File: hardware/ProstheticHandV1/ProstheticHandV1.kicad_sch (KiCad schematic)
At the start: 19 parts, among them J1 Servo_01, J2 Servo_02, J3 Servo_03, J4 Servo_04, J5 JTAG, J6 Bat_Con, J7 OLED_Disp, SW1 Button_01, SW2 Button_02, U1 LM7805_TO220

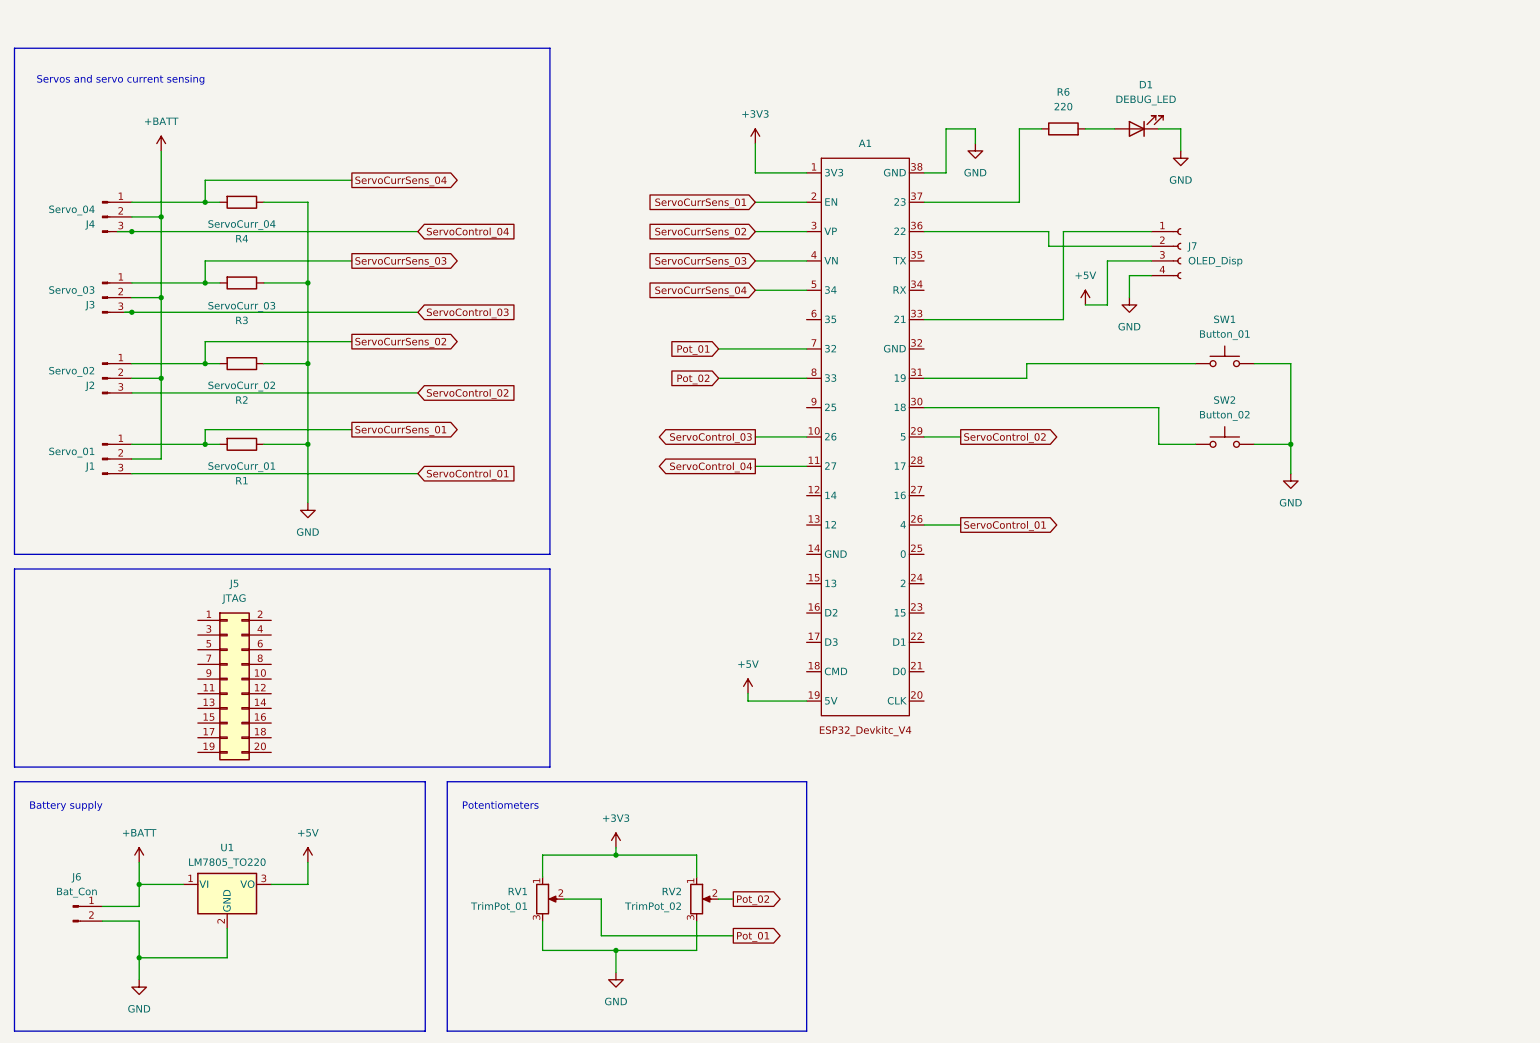
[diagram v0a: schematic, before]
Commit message: KiCAD: Create symbol and footprint for ESP32 S3
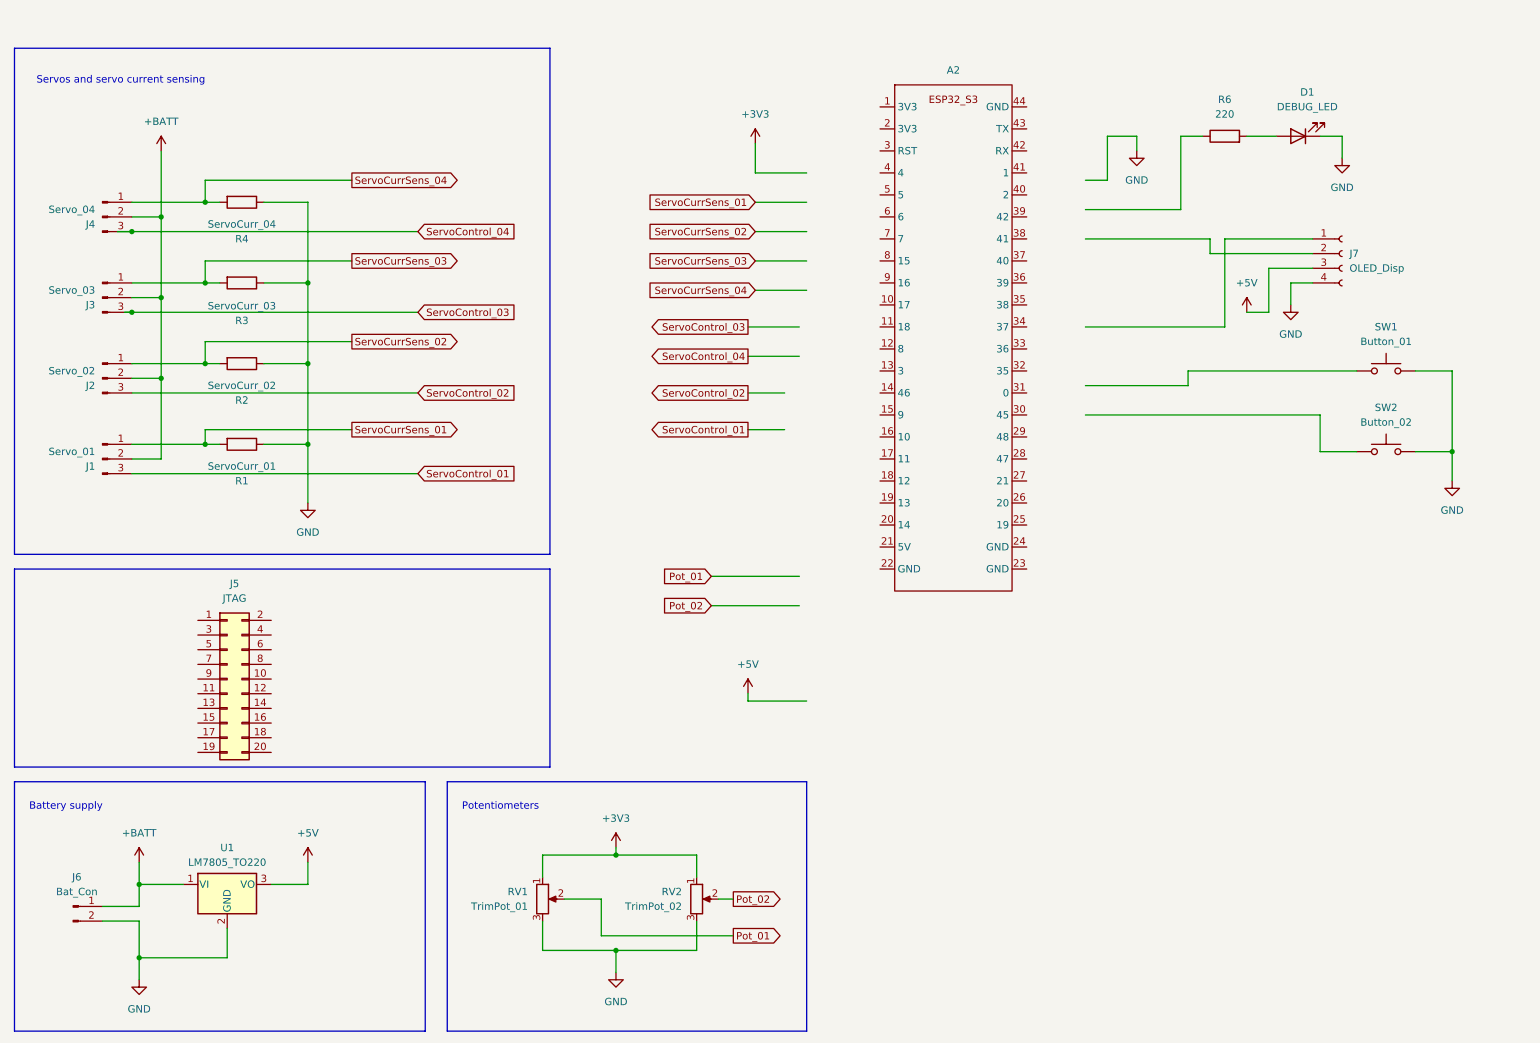
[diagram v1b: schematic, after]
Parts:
- removed A1: ~, symbol ComponentLibrary:ESP32_Devkitc_V4
- added A2: ~, symbol ComponentLibrary:ESP32_S3_DevKitC_V1
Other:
- moved on the sheet: D1, J7, R6, SW1, SW2

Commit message: Started PCB design for hand V1
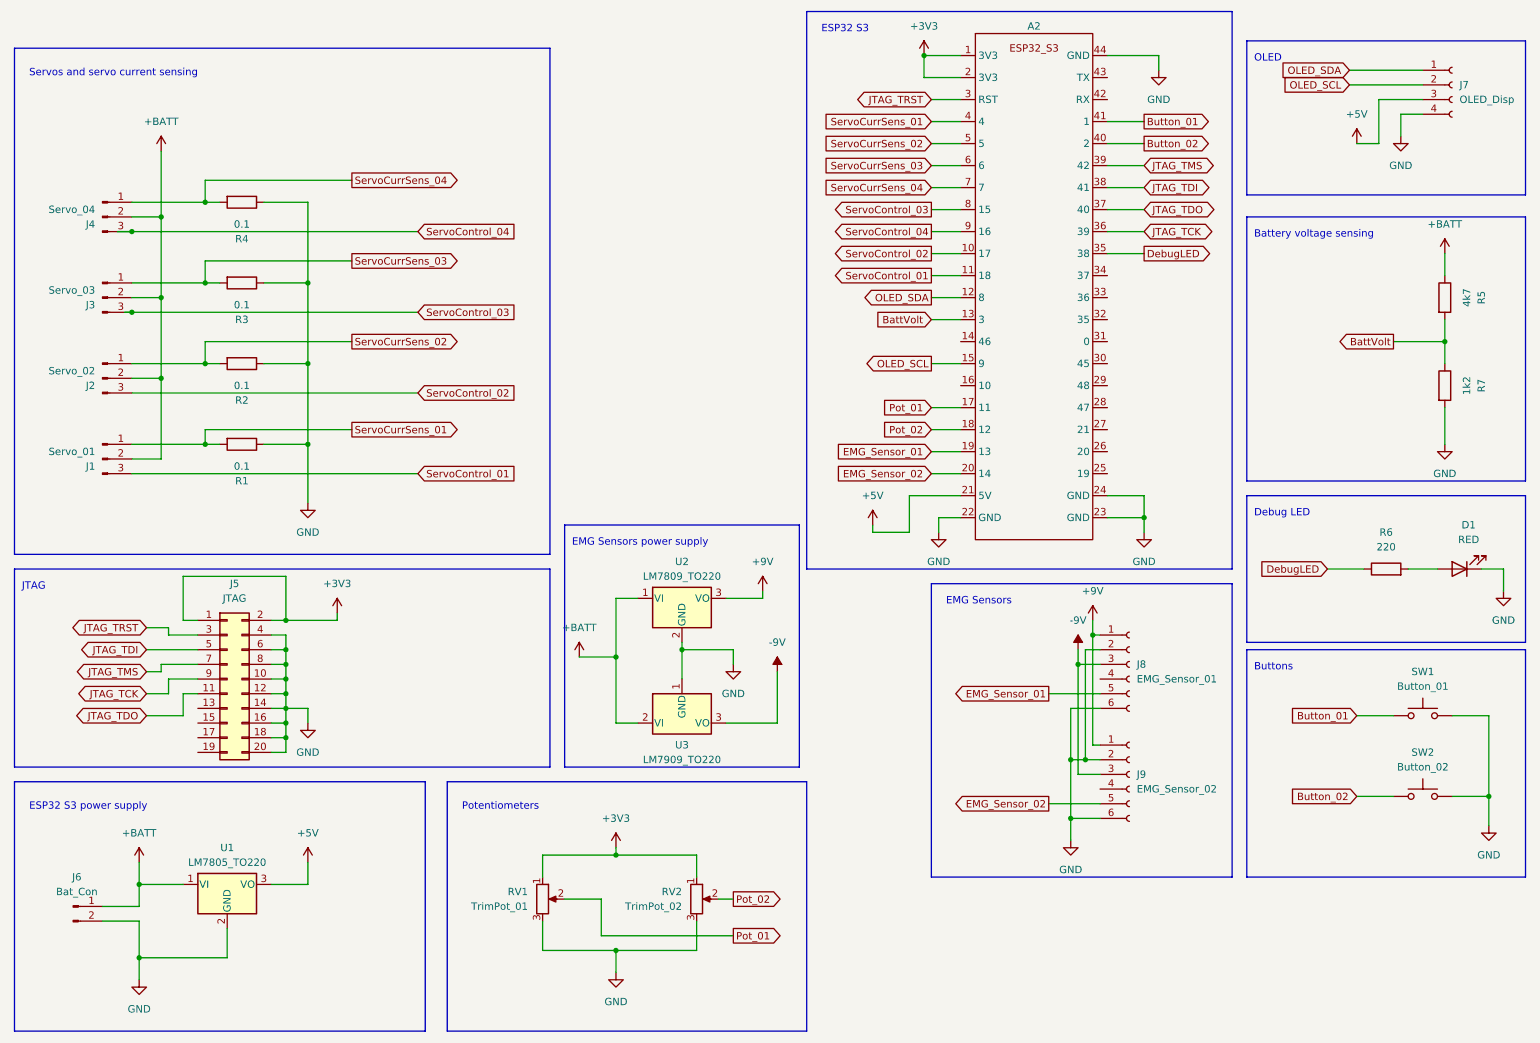
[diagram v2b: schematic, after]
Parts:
- added J8: EMG_Sensor_01, Connector_PinHeader_2.54mm:PinHeader_1x06_P2.54mm_Vertical, symbol Connector:Conn_01x06_Socket
- added J9: EMG_Sensor_02, Connector_PinHeader_2.54mm:PinHeader_1x06_P2.54mm_Vertical, symbol Connector:Conn_01x06_Socket
- added R5: 4k7, Resistor_THT:R_Axial_DIN0207_L6.3mm_D2.5mm_P7.62mm_Horizontal, symbol Device:R
- added R7: 1k2, Resistor_THT:R_Axial_DIN0207_L6.3mm_D2.5mm_P7.62mm_Horizontal, symbol Device:R
- added U2: LM7809_TO220, Package_TO_SOT_THT:TO-220-3_Vertical, symbol Regulator_Linear:LM7809_TO220
- added U3: LM7909_TO220, Package_TO_SOT_THT:TO-220-3_Vertical, symbol Regulator_Linear:LM7909_TO220
- A2: footprint (none) -> MyLibrary:ESP32_S3_DevKitC_V1
- D1: value DEBUG_LED -> RED; footprint (none) -> LED_THT:LED_D5.0mm
- J1, J2, J3, J4: footprint (none) -> Connector_PinHeader_2.54mm:PinHeader_1x03_P2.54mm_Vertical
- J5: footprint (none) -> Connector_PinHeader_2.54mm:PinHeader_2x10_P2.54mm_Vertical
- J6: footprint (none) -> Connector_PinHeader_2.54mm:PinHeader_1x02_P2.54mm_Vertical
- J7: footprint (none) -> Connector_PinHeader_2.54mm:PinHeader_1x04_P2.54mm_Vertical
- R1: value ServoCurr_01 -> 0.1; footprint (none) -> Resistor_THT:R_Axial_Power_L25.0mm_W9.0mm_P27.94mm
- R2: value ServoCurr_02 -> 0.1; footprint (none) -> Resistor_THT:R_Axial_Power_L25.0mm_W9.0mm_P27.94mm
- R3: value ServoCurr_03 -> 0.1; footprint (none) -> Resistor_THT:R_Axial_Power_L25.0mm_W9.0mm_P27.94mm
- R4: value ServoCurr_04 -> 0.1; footprint (none) -> Resistor_THT:R_Axial_Power_L25.0mm_W9.0mm_P27.94mm
- R6: footprint (none) -> Resistor_THT:R_Axial_DIN0207_L6.3mm_D2.5mm_P7.62mm_Horizontal
- RV1, RV2: footprint (none) -> Potentiometer_THT:Potentiometer_Alps_RK163_Single_Horizontal
- SW1, SW2: footprint (none) -> Button_Switch_THT:SW_PUSH_6mm
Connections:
- net +3V3: now also A2.1 (3V3), A2.2 (3V3), J5.1 (Pin_1), J5.2 (Pin_2)
- net +5V: now also A2.21 (5V)
- net +BATT: now also R5.1, U2.1 (VI), U3.2 (VI)
- net GND: now also A2.22 (GND), A2.23 (GND), A2.24 (GND), A2.44 (GND), J5.10 (Pin_10), J5.12 (Pin_12), J5.14 (Pin_14), J5.16 (Pin_16), J5.18 (Pin_18), J5.20 (Pin_20), J5.4 (Pin_4), J5.6 (Pin_6), J5.8 (Pin_8), J8.2 (Pin_2), J8.6 (Pin_6), J9.2 (Pin_2), J9.6 (Pin_6), R7.2, U2.2 (GND), U3.1 (GND)
- net Pot_01: now also A2.17 (11)
- net Pot_02: now also A2.18 (12)
- net ServoControl_01: now also A2.11 (18)
- net ServoControl_02: now also A2.10 (17)
- net ServoControl_03: now also A2.8 (15)
- net ServoControl_04: now also A2.9 (16)
- net ServoCurrSens_01: now also A2.4
- net ServoCurrSens_02: now also A2.5
- net ServoCurrSens_03: now also A2.6
- net ServoCurrSens_04: now also A2.7
- net OLED_SDA: now reaches A2.12 (8)
- net OLED_SDA: now also J7.1 (Pin_1)
- net BattVolt: now reaches A2.13 (3)
- net BattVolt: now also R5.2, R7.1
- net OLED_SCL: now reaches A2.15 (9)
- net OLED_SCL: now also J7.2 (Pin_2)
- net EMG_Sensor_01: now reaches A2.19 (13)
- net EMG_Sensor_01: now also J8.5 (Pin_5)
- net EMG_Sensor_02: now reaches A2.20 (14)
- net EMG_Sensor_02: now also J9.5 (Pin_5)
- net JTAG_TRST: now reaches A2.3 (RST)
- net JTAG_TRST: now also J5.3 (Pin_3)
- net DebugLED: now reaches A2.35 (38)
- net DebugLED: now also R6.1
- net JTAG_TCK: now reaches A2.36 (39)
- net JTAG_TCK: now also J5.9 (Pin_9)
- net JTAG_TDO: now reaches A2.37 (40)
- net JTAG_TDO: now also J5.11 (Pin_11)
- net JTAG_TDI: now reaches A2.38 (41)
- net JTAG_TDI: now also J5.5 (Pin_5)
- net JTAG_TMS: now reaches A2.39 (42)
- net JTAG_TMS: now also J5.7 (Pin_7)
- net Button_02: now reaches A2.40 (2)
- net Button_02: now also SW2.1
- net Button_01: now reaches A2.41 (1)
- net Button_01: now also SW1.1
- new net +9V: J8.1 (Pin_1), J9.1 (Pin_1), U2.3 (VO)
- new net -9V: J8.3 (Pin_3), J9.3 (Pin_3), U3.3 (VO)
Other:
- note added: "Battery voltage sensing"
- note added: "Buttons"
- note added: "Debug LED"
- note added: "EMG Sensors"
- note added: "EMG Sensors power supply"
- note added: "ESP32 S3"
- note added: "ESP32 S3 power supply"
- note added: "JTAG"
- note added: "OLED"
- note removed: "Battery supply"
- moved on the sheet: A2, D1, J7, R6, SW1, SW2

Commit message: Done hand PCB v1
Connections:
- net ServoControl_01: now also A2.8 (15); no longer A2.11 (18)
- net ServoControl_02: now also A2.9 (16); no longer A2.10 (17)
- net ServoControl_03: now also A2.10 (17); no longer A2.8 (15)
- net ServoControl_04: now also A2.11 (18); no longer A2.9 (16)

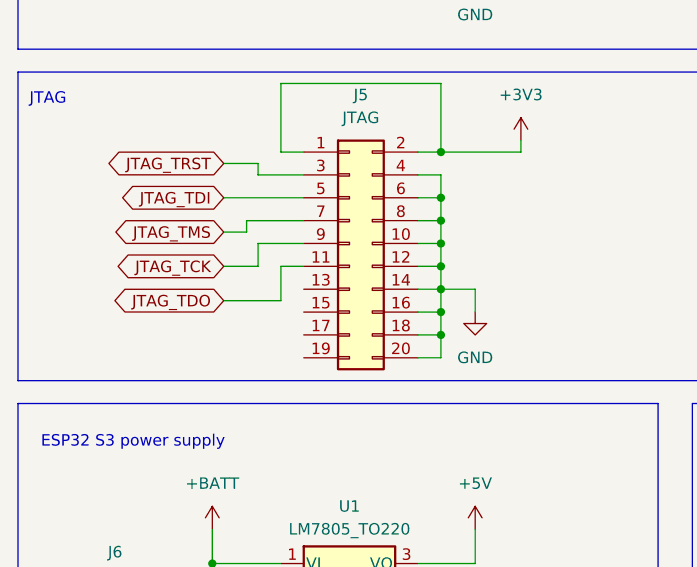
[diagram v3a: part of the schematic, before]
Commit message: Update schematic: jtag fix
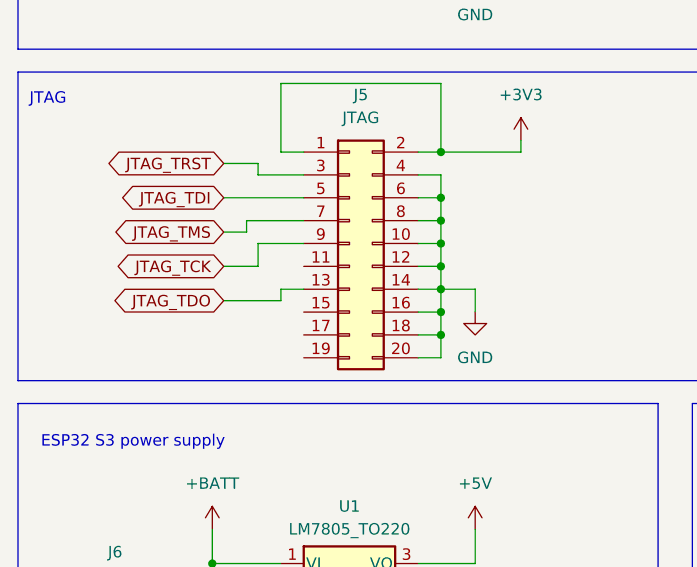
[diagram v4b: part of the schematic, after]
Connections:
- net JTAG_TDO: now also J5.13 (Pin_13); no longer J5.11 (Pin_11)
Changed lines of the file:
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@@
-    (stroke (width 0) (type default))
-  )
-  (wire (pts (xy 48.26 132.08) (xy 50.8 132.08))
     (stroke (width 0) (type default))
   )
@@
     (stroke (width 0) (type default))
   )
+  (wire (pts (xy 48.26 134.62) (xy 50.8 134.62))
+    (stroke (width 0) (type default))
+  )
   (wire (pts (xy 52.07 57.15) (xy 77.47 57.15))
     (stroke (width 0) (type default))
@@
     (stroke (width 0) (type default))
   )
-  (wire (pts (xy 48.26 135.89) (xy 48.26 132.08))
-    (stroke (width 0) (type default))
-  )
+  (wire (pts (xy 48.26 135.89) (xy 48.26 134.62))
+    (stroke (width 0) (type default))
+  )
